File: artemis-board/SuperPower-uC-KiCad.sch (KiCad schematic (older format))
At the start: 5 parts, among them J8 regulator board

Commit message: renamed net lables, disconnected en lines from header and deleted unused
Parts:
- J8: footprint Connector_PinSocket_2.54mm:PinSocket_1x13_P2.54mm_Vertical -> Connector_PinHeader_2.54mm:PinHeader_1x13_P2.54mm_Vertical
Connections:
- net 3v3_EN: no longer names the net of J8.9 (Pin_9)
- net 3v3_MCU_1 renamed 3v3_MCU
- net 5V_EN: no longer names the net of J8.7 (Pin_7)
- net D1+ renamed D+
- net D1- renamed D-
- net SCL_1 renamed SCL
- net SDA_1 renamed SDA
- net VBUS_1 renamed VBUS
- no-connect marks 1 -> 3
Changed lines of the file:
@@
 	8600 3850 8600 3900
 Text Label 8900 3350 0    50   ~ 0
-VBUS_1
+VBUS
 Text Label 8900 3250 0    50   ~ 0
-D1-
+D-
 Wire Wire Line
 	8900 3350 9300 3350
@@
 	8900 3150 9300 3150
 Text Label 8900 3150 0    50   ~ 0
-D1+
+D+
 Text Label 8900 2850 0    50   ~ 0
-SCL_1
+SCL
 Text Label 8900 2950 0    50   ~ 0
-SDA_1
+SDA
 Wire Wire Line
 	8900 2950 9300 2950
@@
 	4300 2500 4800 2500
 Text Label 6300 4100 0    50   ~ 0
-SCL_1
+SCL
 Text Label 6300 4200 0    50   ~ 0
-SDA_1
+SDA
 Wire Wire Line
 	4600 3100 4600 4450
@@
 	6150 4200 6300 4200
 Text Label 4400 2850 0    50   ~ 0
-SCL_1
+SCL
 Text Label 4400 2950 0    50   ~ 0
-SDA_1
+SDA
 Wire Wire Line
 	4400 2850 4300 2850
@@
 	8900 3550 9300 3550
 Text Label 4200 5000 0    50   ~ 0
-VBUS_1
+VBUS
 Wire Wire Line
 	4200 5000 4100 5000
@@
 	4200 4750 4100 4750
 Text Label 8900 3750 0    50   ~ 0
-3v3_MCU_1
+3v3_MCU
 Wire Wire Line
 	8900 3750 9300 3750
 Text Label 6300 2550 0    50   ~ 0
-3v3_MCU_1
+3v3_MCU
 Wire Wire Line
 	6300 2550 6150 2550
-Text GLabel 8900 3650 0    50   Input ~ 0
-3v3_EN
-Text GLabel 8900 3450 0    50   Input ~ 0
-5V_EN
-Wire Wire Line
-	9300 3450 8900 3450
-Wire Wire Line
-	9300 3650 8900 3650
 Text Label 4200 4750 0    50   ~ 0
-D1+
+D+
 Text Label 4200 4850 0    50   ~ 0
-D1-
+D-
 Wire Wire Line
 	8600 3050 8600 3100
@@
 F 0 "J8" H 9550 3500 50  0000 L CNN
 F 1 "regulator board" H 9550 3400 50  0000 L CNN
-F 2 "Connector_PinSocket_2.54mm:PinSocket_1x13_P2.54mm_Vertical" H 9500 3450 50  0001 C CNN
+F 2 "Connector_PinHeader_2.54mm:PinHeader_1x13_P2.54mm_Vertical" H 9500 3450 50  0001 C CNN
 F 3 "~" H 9500 3450 50  0001 C CNN
 	1    9500 3450
@@
 	1    0    0    -1
 $EndComp
+NoConn ~ 9300 3650
+NoConn ~ 9300 3450
 $EndSCHEMATC

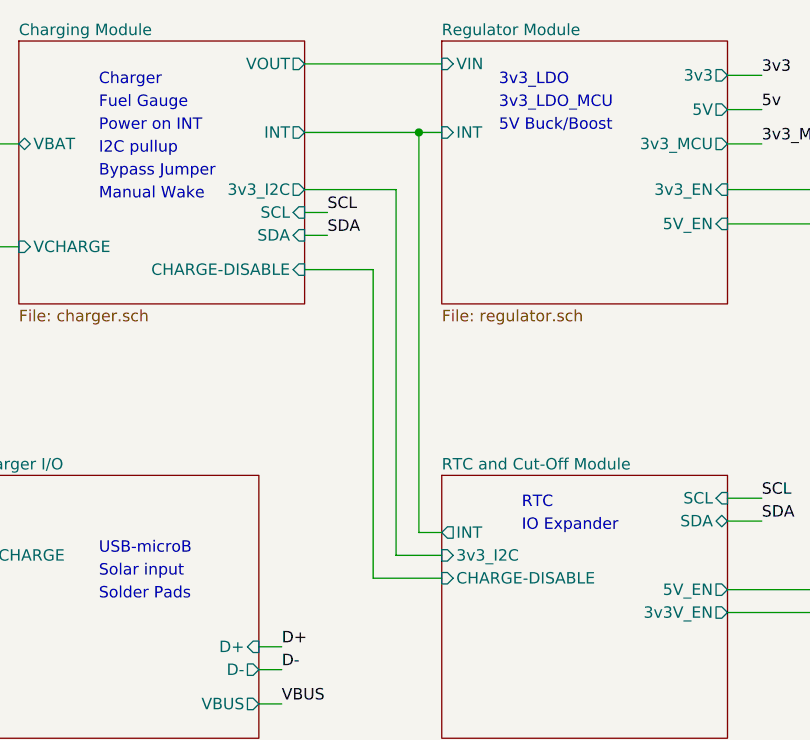
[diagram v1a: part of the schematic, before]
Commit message: connected io expanders Vccp pin to Vbat instead of Vcc_I2c
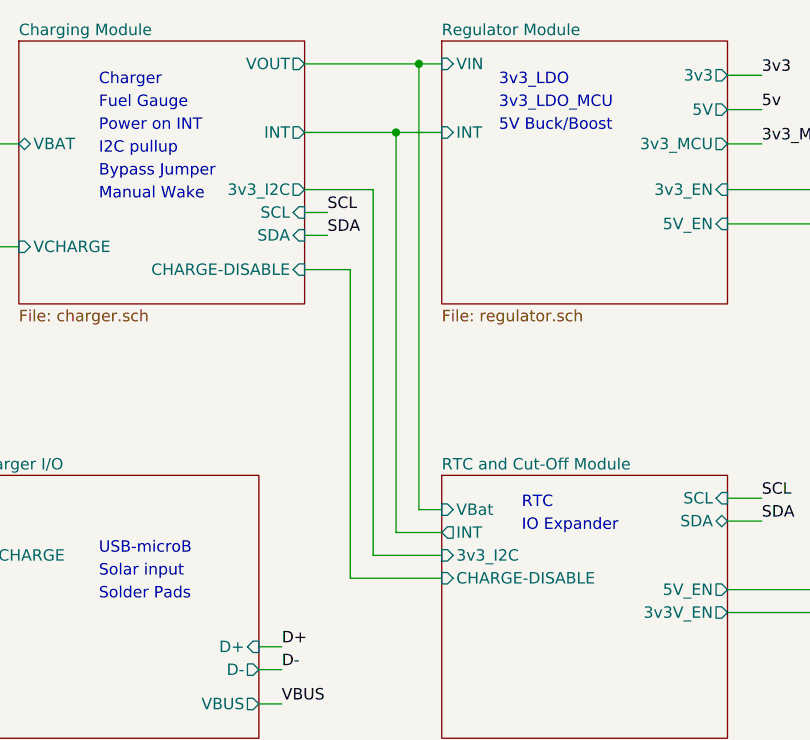
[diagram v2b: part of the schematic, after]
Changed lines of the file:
@@
 	6600 4500 6150 4500
 Wire Wire Line
-	4300 3100 4600 3100
-Wire Wire Line
-	4600 4450 4900 4450
+	4300 3100 4500 3100
+Wire Wire Line
+	4500 4450 4900 4450
 $Sheet
 S 4900 4000 1250 1150
@@
 F7 "3v3V_EN" O R 6150 4600 50
 F8 "3v3_I2C" I L 4900 4350 50
+F9 "VBat" I L 4900 4150 50
 $EndSheet
 $Sheet
@@
 	9300 2850 8900 2850
 Wire Wire Line
-	4300 2500 4800 2500
+	4300 2500 4700 2500
 Text Label 6300 4100 0    50   ~ 0
 SCL
@@
 SDA
 Wire Wire Line
-	4600 3100 4600 4450
+	4500 3100 4500 4450
 Wire Wire Line
 	6300 4100 6150 4100
@@
 NoConn ~ 9300 4050
 Wire Wire Line
-	4300 2200 4900 2200
-Wire Wire Line
-	4900 2500 4800 2500
-Connection ~ 4800 2500
-Wire Wire Line
-	4800 4250 4900 4250
-Wire Wire Line
-	4800 2500 4800 4250
-Wire Wire Line
-	4300 2750 4700 2750
-Wire Wire Line
-	4700 2750 4700 4350
-Wire Wire Line
-	4700 4350 4900 4350
+	4300 2200 4800 2200
+Wire Wire Line
+	4900 2500 4700 2500
+Connection ~ 4700 2500
+Wire Wire Line
+	4700 4250 4900 4250
+Wire Wire Line
+	4700 2500 4700 4250
 Wire Wire Line
 	2550 2550 3050 2550
@@
 NoConn ~ 9300 3650
 NoConn ~ 9300 3450
+Wire Wire Line
+	4600 4350 4900 4350
+Wire Wire Line
+	4300 2750 4600 2750
+Wire Wire Line
+	4600 2750 4600 4350
+Wire Wire Line
+	4900 4150 4800 4150
+Wire Wire Line
+	4800 4150 4800 2200
+Connection ~ 4800 2200
+Wire Wire Line
+	4800 2200 4900 2200
 $EndSCHEMATC

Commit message: added cirquit to measure Vbat with esp in case of fuel gauge shortage
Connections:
- net RTC and Cut-Off Module/Vmeasure: now reaches J8.13 (Pin_13)
- no-connect marks 3 -> 2
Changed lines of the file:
@@
 F8 "3v3_I2C" I L 4900 4350 50
 F9 "VBat" I L 4900 4150 50
+F10 "Vmeasure" O R 6150 4750 50
 $EndSheet
 $Sheet
@@
 Wire Wire Line
 	8600 3850 9300 3850
-NoConn ~ 9300 4050
 Wire Wire Line
 	4300 2200 4800 2200
@@
 Wire Wire Line
 	4800 2200 4900 2200
+Wire Wire Line
+	6150 4750 8950 4750
+Wire Wire Line
+	8950 4750 8950 4050
+Wire Wire Line
+	8950 4050 9300 4050
 $EndSCHEMATC

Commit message: moved Vbat/2 line to other pin on the header
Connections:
- net RTC and Cut-Off Module/Vmeasure: now also J8.9 (Pin_9); no longer J8.13 (Pin_13)
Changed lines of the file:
@@
 	1    0    0    -1
 $EndComp
-NoConn ~ 9300 3650
 NoConn ~ 9300 3450
 Wire Wire Line
@@
 	4800 2200 4900 2200
 Wire Wire Line
-	6150 4750 8950 4750
+	6150 4750 8350 4750
 Wire Wire Line
-	8950 4750 8950 4050
+	8350 4750 8350 3650
 Wire Wire Line
-	8950 4050 9300 4050
+	8350 3650 9300 3650
+NoConn ~ 9300 4050
 $EndSCHEMATC

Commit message: swapped and added some lcsc part numbers and DNP markers
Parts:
- H1, H3, H5, H6: DNP (none) -> DNP
- J8: footprint Connector_PinHeader_2.54mm:PinHeader_1x13_P2.54mm_Vertical -> Connector_PinSocket_2.54mm:PinSocket_1x13_P2.54mm_Vertical; LCSC (none) -> C52709
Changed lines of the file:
@@
 F 0 "J8" H 9550 3500 50  0000 L CNN
 F 1 "regulator board" H 9550 3400 50  0000 L CNN
-F 2 "Connector_PinHeader_2.54mm:PinHeader_1x13_P2.54mm_Vertical" H 9500 3450 50  0001 C CNN
+F 2 "Connector_PinSocket_2.54mm:PinSocket_1x13_P2.54mm_Vertical" H 9500 3450 50  0001 C CNN
 F 3 "~" H 9500 3450 50  0001 C CNN
+F 4 "C52709 " H 9500 3450 50  0001 C CNN "LCSC"
 	1    9500 3450
 	1    0    0    -1
@@
 F 2 "MountingHole:MountingHole_2.7mm_M2.5_ISO7380" H 8050 5950 50  0001 C CNN
 F 3 "~" H 8050 5950 50  0001 C CNN
+F 4 "DNP" H 8050 5950 50  0001 C CNN "DNP"
 	1    8050 5950
 	1    0    0    -1
@@
 F 2 "MountingHole:MountingHole_2.7mm_M2.5_ISO7380" H 8050 5750 50  0001 C CNN
 F 3 "~" H 8050 5750 50  0001 C CNN
+F 4 "DNP" H 8050 5750 50  0001 C CNN "DNP"
 	1    8050 5750
 	1    0    0    -1
@@
 F 2 "MountingHole:MountingHole_2.7mm_M2.5_ISO7380" H 7300 5950 50  0001 C CNN
 F 3 "~" H 7300 5950 50  0001 C CNN
+F 4 "DNP" H 7300 5950 50  0001 C CNN "DNP"
 	1    7300 5950
 	1    0    0    -1
@@
 F 2 "MountingHole:MountingHole_2.7mm_M2.5_ISO7380" H 7300 5750 50  0001 C CNN
 F 3 "~" H 7300 5750 50  0001 C CNN
+F 4 "DNP" H 7300 5750 50  0001 C CNN "DNP"
 	1    7300 5750
 	1    0    0    -1

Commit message: added jumpers for use without io expander
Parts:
- added JP3: jumper, Jumper:SolderJumper-3_P1.3mm_Open_Pad1.0x1.5mm, symbol Jumper:SolderJumper_3_Open
- added JP4: Jumper_NO_Small, Jumper:SolderJumper-2_P1.3mm_Open_Pad1.0x1.5mm, symbol Device:Jumper_NO_Small
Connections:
- net RTC and Cut-Off Module/3v3V_EN: now also JP3.3 (B)
- net RTC and Cut-Off Module/5V_EN: now also JP4.1
- net RTC and Cut-Off Module/Vmeasure: now also JP3.1 (A); no longer J8.9 (Pin_9)
- net at J8.7 (Pin_7): now also JP4.2
- new net: J8.9 (Pin_9), JP3.2 (C)
- no-connect marks 2 -> 1
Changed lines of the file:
@@
 I2C pullup
 Wire Wire Line
-	6650 4600 6650 2750
+	6650 4600 6650 3850
 Wire Wire Line
 	6150 4600 6650 4600
@@
 	6150 2900 6600 2900
 Wire Wire Line
-	6600 2900 6600 4500
+	6600 2900 6600 3450
 Wire Wire Line
 	6600 4500 6150 4500
@@
 	1    0    0    -1
 $EndComp
-NoConn ~ 9300 3450
 Wire Wire Line
 	4600 4350 4900 4350
@@
 	4800 2200 4900 2200
 Wire Wire Line
-	6150 4750 8350 4750
-Wire Wire Line
-	8350 4750 8350 3650
-Wire Wire Line
-	8350 3650 9300 3650
+	6150 4750 8200 4750
 NoConn ~ 9300 4050
+$Comp
+L Device:Jumper_NO_Small JP4
+U 1 1 60D487D3
+P 8000 3450
+F 0 "JP4" H 8000 3635 50  0000 C CNN
+F 1 "Jumper_NO_Small" H 8000 3544 50  0000 C CNN
+F 2 "Jumper:SolderJumper-2_P1.3mm_Open_Pad1.0x1.5mm" H 8000 3450 50  0001 C CNN
+F 3 "~" H 8000 3450 50  0001 C CNN
+	1    8000 3450
+	1    0    0    -1
+$EndComp
+$Comp
+L Jumper:SolderJumper_3_Open JP?
+U 1 1 60D4D872
+P 8000 3850
+AR Path="/5F63B107/60D4D872" Ref="JP?"  Part="1"
+AR Path="/60D4D872" Ref="JP3"  Part="1"
+F 0 "JP3" H 7850 3800 50  0000 C CNN
+F 1 "jumper" H 8050 3950 50  0000 C CNN
+F 2 "Jumper:SolderJumper-3_P1.3mm_Open_Pad1.0x1.5mm" H 8000 3850 50  0001 C CNN
+F 3 "~" H 8000 3850 50  0001 C CNN
+F 4 "DNP" H 8000 3850 50  0001 C CNN "DNP"
+	1    8000 3850
+	-1   0    0    1
+$EndComp
+Wire Wire Line
+	8200 3850 8200 4750
+Wire Wire Line
+	8000 3650 8000 3700
+Wire Wire Line
+	8000 3650 9300 3650
+Wire Wire Line
+	9300 3450 8100 3450
+Wire Wire Line
+	7900 3450 6600 3450
+Connection ~ 6600 3450
+Wire Wire Line
+	6600 3450 6600 4500
+Wire Wire Line
+	7800 3850 6650 3850
+Connection ~ 6650 3850
+Wire Wire Line
+	6650 3850 6650 2750
 $EndSCHEMATC

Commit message: added comments for the jumpers and pulldowns for Q7 and Q8
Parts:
- JP4: value Jumper_NO_Small -> Jumper 5v enable
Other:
- note added: "JP3 position 1 for voltage measuring (requires io expander)\nposition 3 only if IO expander is not populated"
- note added: "use JP4 only if IO expander is not populated"
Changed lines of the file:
@@
 P 8000 3450
 F 0 "JP4" H 8000 3635 50  0000 C CNN
-F 1 "Jumper_NO_Small" H 8000 3544 50  0000 C CNN
+F 1 "Jumper 5v enable" H 8000 3544 50  0000 C CNN
 F 2 "Jumper:SolderJumper-2_P1.3mm_Open_Pad1.0x1.5mm" H 8000 3450 50  0001 C CNN
 F 3 "~" H 8000 3450 50  0001 C CNN
@@
 Wire Wire Line
 	6650 3850 6650 2750
+Text Notes 6700 3150 0    50   ~ 0
+use JP4 only if IO expander is not populated
+Text Notes 6950 4950 0    50   ~ 0
+JP3 position 1 for voltage measuring (requires io expander)\nposition 3 only if IO expander is not populated
 $EndSCHEMATC
